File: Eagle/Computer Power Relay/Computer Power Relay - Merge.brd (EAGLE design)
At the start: 129.9 x 78 mm, 43 parts, among them K1 RELAY-3V3DC-110VAC012, K2 RELAY-110VACV3_IN-PLACE, U1 RP2040, U2 AP2112M-3.3TRG1

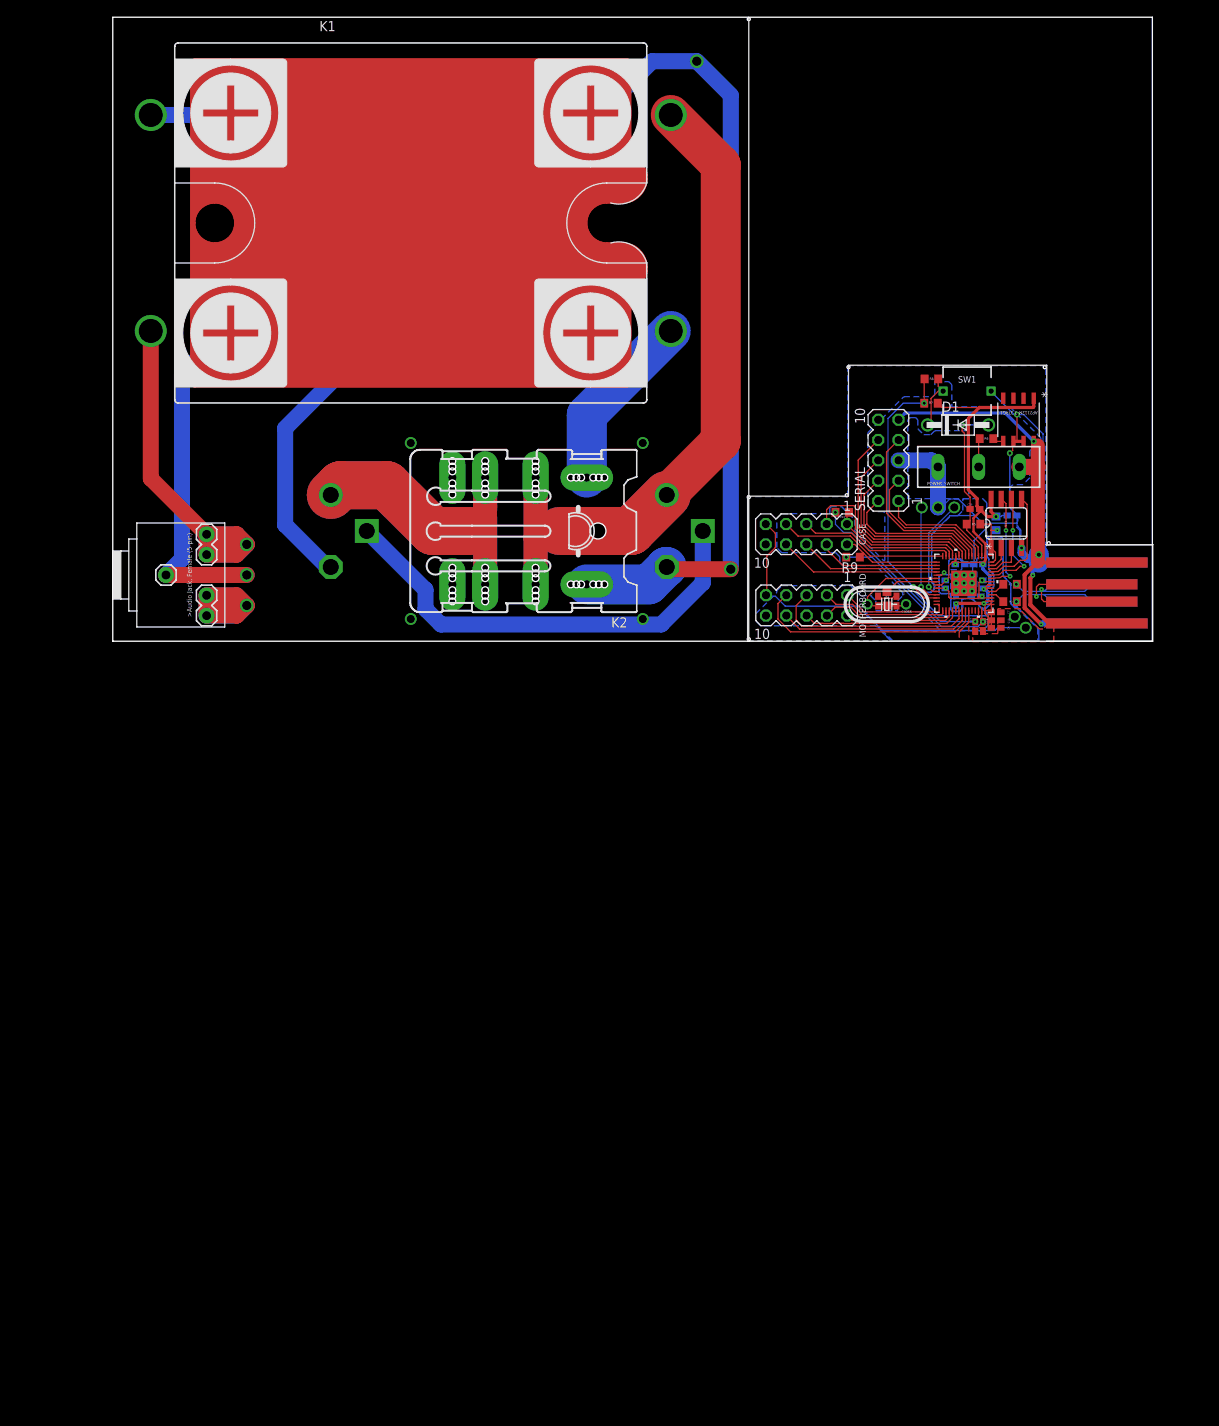
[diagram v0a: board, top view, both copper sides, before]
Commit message: (CPR) 90% done, almost ready to send to fab
Power Strip board is 100% complete.
Controller board is 95% complete, all that's left is to figure out a method to restart into Boot Select with a single button press, and double-check that it works before sending it off to print.

Remaining space of board is being filled out, and is nearly finished.

I'm considering adding plated holes for spacer holes into the Power Strip board.  We'll see.
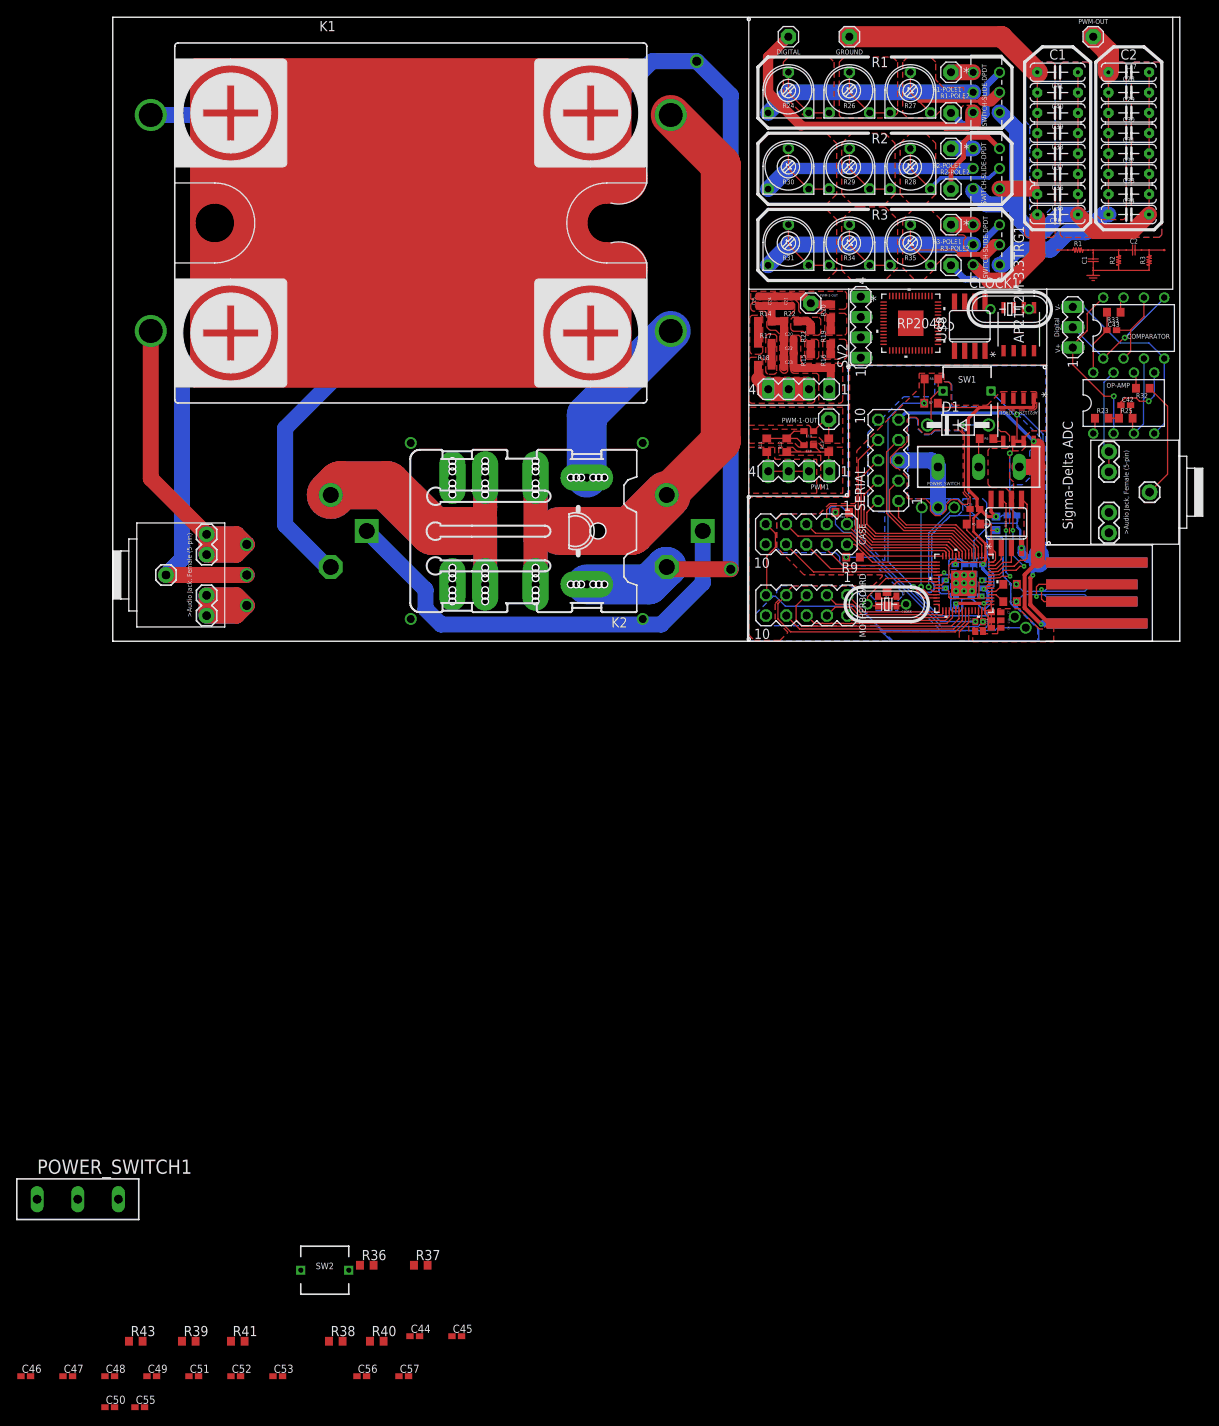
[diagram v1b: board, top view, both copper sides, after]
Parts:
- added C18, C20, C22, C23, C46, C47, C48, C49, C51, C52, C53, C56, C57: 100nF, adafruit:C0402K
- added C19, C21, C24, C25: 47uF, adafruit:C0402K
- added C26, C27, C28, C29, C30, C31, C32, C33, C34, C35, C36, C37, C38, C39, C40, C41: (no value), Inventory:CAPACITOR-CERAMIC
- added C42, C43: (no value), adafruit:C0402K
- added C44, C45: ~30pF, adafruit:C0402K
- added C50, C55: 1uF, adafruit:C0402K
- added CLOCK1: 12MHz, crystal:HC49/S
- added COMPARATOR: COMPARATOR_LM393N, Inventory:IC_2*4(8-PIN)
- added DIGITAL, GROUND, PWM-1-OUT, PWM-2-OUT, PWM-OUT, R1-POLE1, R1-POLE2, R2-POLE1, R2-POLE2, R3-POLE1, R3-POLE2: (no value), adafruit:1X01
- added OP-AMP: OP-AMP_TDA2822N, Inventory:IC_2*4(8-PIN)
- added POWER_SWITCH1: SWITCH-SLIDE-2P2T, Inventory:SWITCH-SLIDE-2P2T
- added PWM1, PWM2, SV2: (no value), con-lstb:MA04-1
- added R11, R14, R17, R18: 220 Ω, rcl:R0603
- added R12, R15, R21, R22: 100 Ω, rcl:R0603
- added R13, R16, R19, R20: 1.8K Ω, rcl:R0603
- added R23, R25, R32, R33: (no value), rcl:R0603
- added R24, R30, R31: 1MΩ, Inventory:POTENTIOMETER_NORMAL
- added R26, R29, R34: 10KΩ, Inventory:POTENTIOMETER_NORMAL
- added R27, R28, R35: 100Ω, Inventory:POTENTIOMETER_NORMAL
- added R36, R37: 27.4 Ω, rcl:R0603
- added R38, R40: 1k Ω, rcl:R0603
- added R39, R41: 10k Ω, rcl:R0603
- added R43: 4.7k Ω, rcl:R0603
- added SV1: (no value), con-lstb:MA03-1
- added SW2: (no value), KVM Keyboard:PUSHBUTTON_TH
- added U$6: AUDIO_JACK_FEMALE_5-PIN, Inventory:AUDIO_JACK_FEMALE_5-PIN
- added U$8: W25Q128JVSIM-ND__QSPI-FLASH, KVM Keyboard:SO08
- added U3, U4, U5: SWITCH-SLIDE-DPDT, Inventory:SWITCH-SLIDE-DPDT
- added U6: RP2040, KVM Keyboard:IC57_RP2040
- added U7: AP2112M-3.3TRG1, KVM Keyboard:AP2112M-3.3TRG1_DIO
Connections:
- new net 5V_2: POWER_SWITCH1.1, SV2.1, U7.8
- new net D+_2: R36.2, SV2.3
- new net D-_2: R37.2, SV2.2
- new net DIGITAL: COMPARATOR.1, COMPARATOR.5, SV1.2
- new net GND-3: C18.2, PWM1.1, R12.2, R13.2
- new net GND-4: C20.2, C22.2, C23.2, PWM2.1, R15.2, R16.2
- new net GND-5: C26.2, C35.2, C36.2, C37.2, C38.2, C39.2, C40.2, C41.2, GROUND.1, U4.4, U5.3
- new net GND-6: C43.2, COMPARATOR.2, COMPARATOR.6, R32.1, U$6.3
- new net GND-7: POWER_SWITCH1.3, SV2.4, U7.6, U7.7
- new net N$10: C19.1, PWM-1-OUT.1, R13.1
- new net N$11: C20.1, C21.2, C22.1, C23.1, C24.2, C25.2, R14.1, R22.1
- new net N$12: C21.1, C24.1, C25.1, PWM-2-OUT.1, R20.1
- new net N$13: R17.1, R18.1
- new net N$14: R14.2, R17.2
- new net N$15: R19.2, R20.2
- new net N$21: R16.1, R19.1
- new net N$22: R15.1, R21.1
- new net N$23: R21.2, R22.2
- new net N$24: DIGITAL.1, U3.3
- new net N$25: R24.2, R24.3, R26.1
- new net N$26: C27.1, C28.1, C29.1, C30.1, C31.1, C32.1, C33.1, C34.1, PWM-OUT.1, U5.4
- new net N$27: R26.2, R26.3, R27.1
- new net N$28: R27.2, R27.3, U3.5
- new net N$29: R24.1, U3.2
- new net N$30: R1-POLE1.1, U3.1
- new net N$31: R1-POLE2.1, U3.6
- new net N$32: R2-POLE2.1, U4.6
- new net N$33: R2-POLE1.1, U4.1
- new net N$34: R30.1, U4.2
- new net N$35: R28.2, R28.3, U4.5
- new net N$36: R3-POLE2.1, U5.6
- new net N$37: R3-POLE1.1, U5.1
- new net N$38: R28.1, R29.2, R29.3
- new net N$39: R29.1, R30.2, R30.3
- new net N$40: R31.1, U5.2
- new net N$41: R34.2, R34.3, R35.1
- new net N$42: R31.2, R31.3, R34.1
- new net N$43: R35.2, R35.3, U5.5
- new net N$44: C26.1, C27.2, C28.2, C29.2, C30.2, C31.2, C32.2, C33.2, C34.2, C35.1, C36.1, C37.1, C38.1, C39.1, C40.1, C41.1, U3.4, U4.3
- new net N$45: OP-AMP.7, U$6.4, U$6.5
- new net N$46: R36.1, U6.47
- new net N$47: OP-AMP.6, R32.2
- new net N$51: C43.1, OP-AMP.8, R33.2
- new net N$52: OP-AMP.1, R23.1
- new net N$53: C42.1, OP-AMP.5, R23.2, R25.1
- new net N$54: C42.2, COMPARATOR.3, OP-AMP.3, R25.2
- new net N$55: R37.1, U6.46
- new net N$56: COMPARATOR.7, R33.1
- new net N$57: C45.2, CLOCK1.2, R38.1
- new net N$58: R38.2, U6.21
- new net N$59: C44.2, CLOCK1.1, U6.20
- new net N$6: PWM1.2, PWM1.3, PWM1.4, R11.2
- new net N$60: U$8.3, U6.54
- new net N$61: U$8.2, U6.55
- new net N$62: U$8.5, U6.53
- new net N$63: U$8.6, U6.52
- new net N$64: U$8.7, U6.51
- new net N$7: C18.1, C19.2, R11.1, R12.1
- new net N$8: PWM2.2, PWM2.3, PWM2.4, R18.2
- new net SD-V+: COMPARATOR.8, OP-AMP.2, SV1.1
- new net SD-V-: COMPARATOR.4, OP-AMP.4, SV1.3
- net 1V1: now also C55.2, C56.2, C57.2, U6.23, U6.45, U6.50
- net 3V3: now also C46.2, C47.2, C48.2, C49.2, C50.2, C51.2, C52.2, C53.2, R39.2, U$8.8, U6.1, U6.10, U6.22, U6.33, U6.42, U6.43, U6.44, U6.48, U6.49, U7.1
- net BOOTSEL: now also R40.2
- net BUTTON: now also R43.1, SW2.P$1
- net EN: now also R41.2, U7.5
- net GND: now also C44.1, C45.1, C46.1, C47.1, C48.1, C49.1, C50.1, C51.1, C52.1, C53.1, C55.1, C56.1, C57.1, SW2.P$2, U$8.4, U6.19, U6.57
- net QSPI_SS_N: now also R39.1, R40.1, U$8.1, U6.56
- net RUN: now also R43.2, U6.26
- net SWITCH: now also POWER_SWITCH1.2, R41.1
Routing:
- net N$44: track 0.00 -> 76.3 mm
- net GND-5: track 0.00 -> 63.4 mm
- net N$48: track 0.00 -> 43.6 mm
- net N$26: track 0.00 -> 39.2 mm
- net N$24: track 0.00 -> 36.8 mm
- net N$40: track 0.00 -> 26.7 mm
- net N$34: track 0.00 -> 26.7 mm
- net N$29: track 0.00 -> 26.7 mm
- net GND-6: track 0.00 -> 25.3 mm
- net SD-V-: track 0.00 -> 24.0 mm
- net SD-V+: track 0.00 -> 21.4 mm, vias 0 -> 1
- net N$43: track 0.00 -> 17.4 mm
- net N$28: track 0.00 -> 16.7 mm
- net DIGITAL: track 0.00 -> 16.3 mm, vias 0 -> 1
- net N$35: track 0.00 -> 15.9 mm
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- added copper zone on layer 1, net GND-3
- added copper zone on layer 1, net GND-4
- added copper zone on layer 1, net GND-5
- added copper zone on layer 16, net GND-5
- added copper zone on layer 1, net N$10
- added copper zone on layer 1, net N$11
- added copper zone on layer 1, net N$12
- added copper zone on layer 1, net N$13
- added copper zone on layer 1, net N$14
- added copper zone on layer 1, net N$15
- added copper zone on layer 1, net N$21
- added copper zone on layer 1, net N$22
- added copper zone on layer 1, net N$23
- added copper zone on layer 1, net N$24
- added copper zone on layer 1, net N$25
- added copper zone on layer 1, net N$26
- added copper zone on layer 16, net N$26
- added copper zone on layer 1, net N$27
- added copper zone on layer 1, net N$28
- added copper zone on layer 1, net N$35
- added copper zone on layer 1, net N$38
- added copper zone on layer 1, net N$39
- added copper zone on layer 1, net N$41
- added copper zone on layer 1, net N$42
- added copper zone on layer 1, net N$43
- added copper zone on layer 1, net N$44
- added copper zone on layer 16, net N$44
- added copper zone on layer 1, net N$6
- added copper zone on layer 1, net N$7
- added copper zone on layer 1, net N$8
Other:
- board size 129.9 x 78 mm -> 133.4 x 78 mm
- board text added: "C1"
- board text added: "C2"
- board text added: "Digital"
- board text added: "R1"
- board text added: "R2"
- board text added: "R3"
- board text added: "RPi Pico recommended values PWM"
- board text added: "Sigma-Delta ADC"
- board text added: "V+"
- board text added: "V-"

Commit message: CPR 100% Complete
Damn shipping's expensive.  Better work on the other projects so I can subsidize this.
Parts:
- removed C18, C20, C22, C23, C46, C47, C48, C49, C51, C52, C53, C56, C57: 100nF, adafruit:C0402K
- removed C19, C21, C24, C25: 47uF, adafruit:C0402K
- removed C26, C27, C28, C29, C30, C31, C32, C33, C34, C35, C36, C37, C38, C39, C40, C41: (no value), Inventory:CAPACITOR-CERAMIC
- removed C42, C43: (no value), adafruit:C0402K
- removed C44, C45: ~30pF, adafruit:C0402K
- removed C50, C55: 1uF, adafruit:C0402K
- removed CLOCK1: 12MHz, crystal:HC49/S
- removed COMPARATOR: COMPARATOR_LM393N, Inventory:IC_2*4(8-PIN)
- removed DIGITAL, GROUND, PWM-1-OUT, PWM-2-OUT, PWM-OUT, R1-POLE1, R1-POLE2, R2-POLE1, R2-POLE2, R3-POLE1, R3-POLE2: (no value), adafruit:1X01
- removed OP-AMP: OP-AMP_TDA2822N, Inventory:IC_2*4(8-PIN)
- removed POWER_SWITCH1: SWITCH-SLIDE-2P2T, Inventory:SWITCH-SLIDE-2P2T
- removed PWM1, PWM2, SV2: (no value), con-lstb:MA04-1
- removed R11, R14, R17, R18: 220 Ω, rcl:R0603
- removed R12, R15, R21, R22: 100 Ω, rcl:R0603
- removed R13, R16, R19, R20: 1.8K Ω, rcl:R0603
- removed R23, R25, R32, R33: (no value), rcl:R0603
- removed R24, R30, R31: 1MΩ, Inventory:POTENTIOMETER_NORMAL
- removed R26, R29, R34: 10KΩ, Inventory:POTENTIOMETER_NORMAL
- removed R27, R28, R35: 100Ω, Inventory:POTENTIOMETER_NORMAL
- removed R36, R37: 27.4 Ω, rcl:R0603
- removed R38, R40: 1k Ω, rcl:R0603
- removed R39, R41: 10k Ω, rcl:R0603
- removed R43: 4.7k Ω, rcl:R0603
- removed SV1: (no value), con-lstb:MA03-1
- removed SW2: (no value), KVM Keyboard:PUSHBUTTON_TH
- removed U$6: AUDIO_JACK_FEMALE_5-PIN, Inventory:AUDIO_JACK_FEMALE_5-PIN
- removed U$8: W25Q128JVSIM-ND__QSPI-FLASH, KVM Keyboard:SO08
- removed U3, U4, U5: SWITCH-SLIDE-DPDT, Inventory:SWITCH-SLIDE-DPDT
- removed U6: RP2040, KVM Keyboard:IC57_RP2040
- removed U7: AP2112M-3.3TRG1, KVM Keyboard:AP2112M-3.3TRG1_DIO
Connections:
- removed net 5V_2: POWER_SWITCH1.1, SV2.1, U7.8
- removed net D+_2: R36.2, SV2.3
- removed net D-_2: R37.2, SV2.2
- removed net DIGITAL: COMPARATOR.1, COMPARATOR.5, SV1.2
- removed net GND-3: C18.2, PWM1.1, R12.2, R13.2
- removed net GND-4: C20.2, C22.2, C23.2, PWM2.1, R15.2, R16.2
- removed net GND-5: C26.2, C35.2, C36.2, C37.2, C38.2, C39.2, C40.2, C41.2, GROUND.1, U4.4, U5.3
- removed net GND-6: C43.2, COMPARATOR.2, COMPARATOR.6, R32.1, U$6.3
- removed net GND-7: POWER_SWITCH1.3, SV2.4, U7.6, U7.7
- removed net N$10: C19.1, PWM-1-OUT.1, R13.1
- removed net N$11: C20.1, C21.2, C22.1, C23.1, C24.2, C25.2, R14.1, R22.1
- removed net N$12: C21.1, C24.1, C25.1, PWM-2-OUT.1, R20.1
- removed net N$13: R17.1, R18.1
- removed net N$14: R14.2, R17.2
- removed net N$15: R19.2, R20.2
- removed net N$21: R16.1, R19.1
- removed net N$22: R15.1, R21.1
- removed net N$23: R21.2, R22.2
- removed net N$24: DIGITAL.1, U3.3
- removed net N$25: R24.2, R24.3, R26.1
- removed net N$26: C27.1, C28.1, C29.1, C30.1, C31.1, C32.1, C33.1, C34.1, PWM-OUT.1, U5.4
- removed net N$27: R26.2, R26.3, R27.1
- removed net N$28: R27.2, R27.3, U3.5
- removed net N$29: R24.1, U3.2
- removed net N$30: R1-POLE1.1, U3.1
- removed net N$31: R1-POLE2.1, U3.6
- removed net N$32: R2-POLE2.1, U4.6
- removed net N$33: R2-POLE1.1, U4.1
- removed net N$34: R30.1, U4.2
- removed net N$35: R28.2, R28.3, U4.5
- removed net N$36: R3-POLE2.1, U5.6
- removed net N$37: R3-POLE1.1, U5.1
- removed net N$38: R28.1, R29.2, R29.3
- removed net N$39: R29.1, R30.2, R30.3
- removed net N$40: R31.1, U5.2
- removed net N$41: R34.2, R34.3, R35.1
- removed net N$42: R31.2, R31.3, R34.1
- removed net N$43: R35.2, R35.3, U5.5
- removed net N$44: C26.1, C27.2, C28.2, C29.2, C30.2, C31.2, C32.2, C33.2, C34.2, C35.1, C36.1, C37.1, C38.1, C39.1, C40.1, C41.1, U3.4, U4.3
- removed net N$45: OP-AMP.7, U$6.4, U$6.5
- removed net N$46: R36.1, U6.47
- removed net N$47: OP-AMP.6, R32.2
- removed net N$51: C43.1, OP-AMP.8, R33.2
- removed net N$52: OP-AMP.1, R23.1
- removed net N$53: C42.1, OP-AMP.5, R23.2, R25.1
- removed net N$54: C42.2, COMPARATOR.3, OP-AMP.3, R25.2
- removed net N$55: R37.1, U6.46
- removed net N$56: COMPARATOR.7, R33.1
- removed net N$57: C45.2, CLOCK1.2, R38.1
- removed net N$58: R38.2, U6.21
- removed net N$59: C44.2, CLOCK1.1, U6.20
- removed net N$6: PWM1.2, PWM1.3, PWM1.4, R11.2
- removed net N$60: U$8.3, U6.54
- removed net N$61: U$8.2, U6.55
- removed net N$62: U$8.5, U6.53
- removed net N$63: U$8.6, U6.52
- removed net N$64: U$8.7, U6.51
- removed net N$7: C18.1, C19.2, R11.1, R12.1
- removed net N$8: PWM2.2, PWM2.3, PWM2.4, R18.2
- removed net SD-V+: COMPARATOR.8, OP-AMP.2, SV1.1
- removed net SD-V-: COMPARATOR.4, OP-AMP.4, SV1.3
- net 1V1: no longer C55.2, C56.2, C57.2, U6.23, U6.45, U6.50
- net 3V3: no longer C46.2, C47.2, C48.2, C49.2, C50.2, C51.2, C52.2, C53.2, R39.2, U$8.8, U6.1, U6.10, U6.22, U6.33, U6.42, U6.43, U6.44, U6.48, U6.49, U7.1
- net BOOTSEL: no longer R40.2
- net BUTTON: no longer R43.1, SW2.P$1
- net EN: no longer R41.2, U7.5
- net GND: no longer C44.1, C45.1, C46.1, C47.1, C48.1, C49.1, C50.1, C51.1, C52.1, C53.1, C55.1, C56.1, C57.1, SW2.P$2, U$8.4, U6.19, U6.57
- net QSPI_SS_N: no longer R39.1, R40.1, U$8.1, U6.56
- net RUN: no longer R43.2, U6.26
- net SWITCH: no longer POWER_SWITCH1.2, R41.1
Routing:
- net N$44: track 76.3 -> 0.00 mm
- net GND-5: track 63.4 -> 0.00 mm
- net N$48: track 43.6 -> 0.00 mm
- net N$26: track 39.2 -> 0.00 mm
- net N$24: track 36.8 -> 0.00 mm
- net N$40: track 26.7 -> 0.00 mm
- net N$34: track 26.7 -> 0.00 mm
- net N$29: track 26.7 -> 0.00 mm
- net GND-6: track 25.3 -> 0.00 mm
- net SD-V-: track 24.0 -> 0.00 mm
- net SD-V+: track 21.4 -> 0.00 mm, vias 1 -> 0
- net N$43: track 17.4 -> 0.00 mm
- net N$28: track 16.7 -> 0.00 mm
- net DIGITAL: track 16.3 -> 0.00 mm, vias 1 -> 0
- net N$35: track 15.9 -> 0.00 mm
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- removed copper zone on layer 1, net GND-3
- removed copper zone on layer 1, net GND-4
- removed copper zone on layer 1, net GND-5
- removed copper zone on layer 16, net GND-5
- removed copper zone on layer 1, net N$10
- removed copper zone on layer 1, net N$11
- removed copper zone on layer 1, net N$12
- removed copper zone on layer 1, net N$13
- removed copper zone on layer 1, net N$14
- removed copper zone on layer 1, net N$15
- removed copper zone on layer 1, net N$21
- removed copper zone on layer 1, net N$22
- removed copper zone on layer 1, net N$23
- removed copper zone on layer 1, net N$24
- removed copper zone on layer 1, net N$25
- removed copper zone on layer 1, net N$26
- removed copper zone on layer 16, net N$26
- removed copper zone on layer 1, net N$27
- removed copper zone on layer 1, net N$28
- removed copper zone on layer 1, net N$35
- removed copper zone on layer 1, net N$38
- removed copper zone on layer 1, net N$39
- removed copper zone on layer 1, net N$41
- removed copper zone on layer 1, net N$42
- removed copper zone on layer 1, net N$43
- removed copper zone on layer 1, net N$44
- removed copper zone on layer 16, net N$44
- removed copper zone on layer 1, net N$6
- removed copper zone on layer 1, net N$7
- removed copper zone on layer 1, net N$8
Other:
- board size 133.4 x 78 mm -> 129.9 x 78 mm
- board text removed: "C1"
- board text removed: "C2"
- board text removed: "Digital"
- board text removed: "R1"
- board text removed: "R2"
- board text removed: "R3"
- board text removed: "RPi Pico recommended values PWM"
- board text removed: "Sigma-Delta ADC"
- board text removed: "V+"
- board text removed: "V-"
